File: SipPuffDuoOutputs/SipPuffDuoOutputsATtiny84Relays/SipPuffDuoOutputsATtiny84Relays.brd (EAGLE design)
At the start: 48 x 70 mm, 19 parts, among them U1 ATTINY84-20PU, U2 AQY212EH, U3 AQY212EH

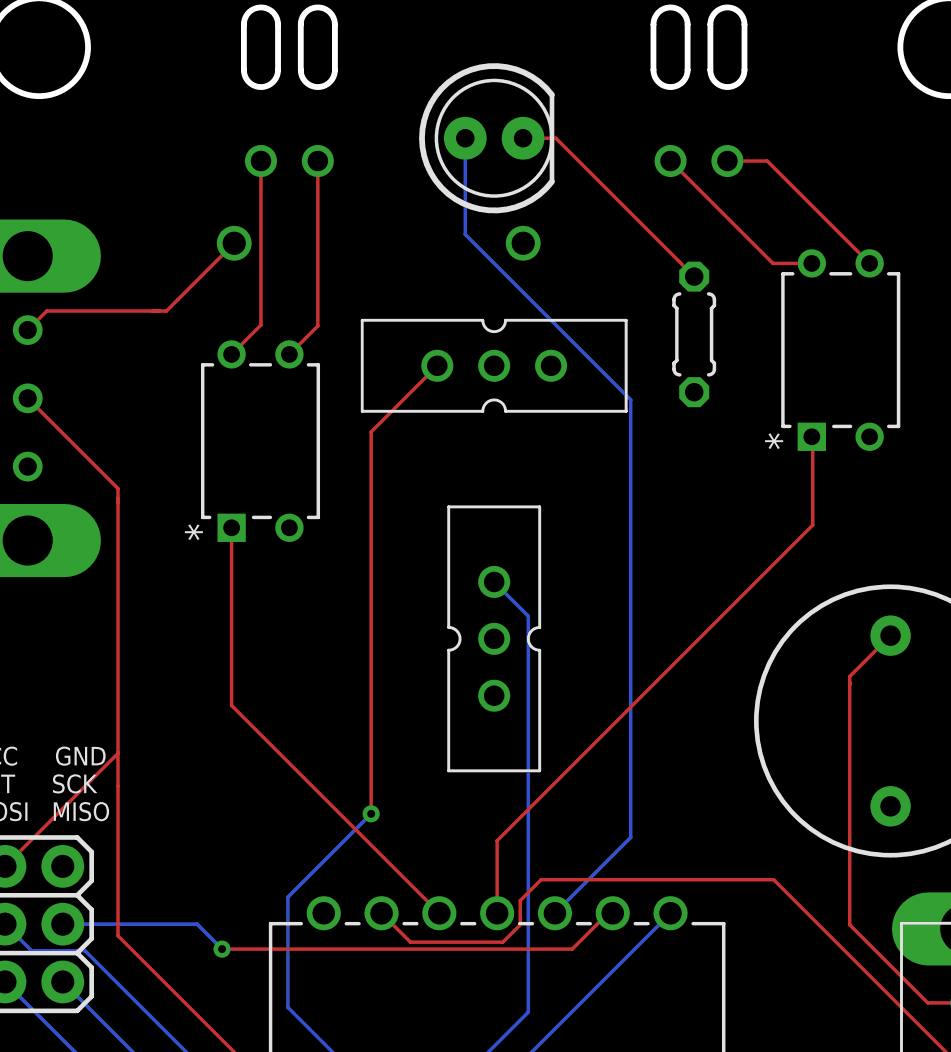
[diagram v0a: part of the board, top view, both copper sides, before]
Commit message: Changed resistors size
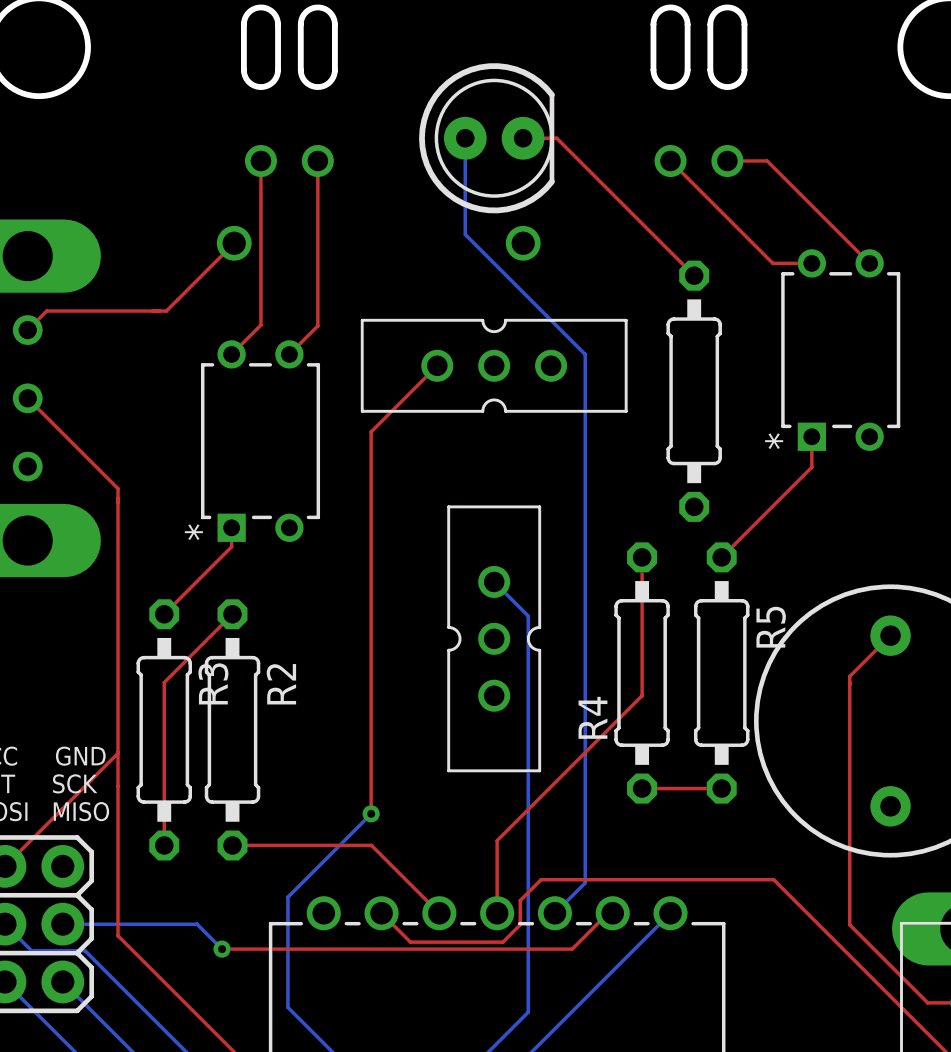
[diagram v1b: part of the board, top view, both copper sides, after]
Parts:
- added R2, R3, R4, R5: 1k, MMC Eagle:RESISTOR_0207/10
- R1: device MMC Eagle:RESISTOR_0204/5 -> MMC Eagle:RESISTOR_0207/10
- moved R1 2.50 mm to (32.8, 50.9)
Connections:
- new net N$19: R2.1, R3.2
- new net N$20: R3.1, U2.1
- new net N$21: R4.1, R5.2
- new net N$22: R5.1, U3.1
- net N$2: now also R2.2; no longer U2.1
- net N$4: now also R4.2; no longer U3.1
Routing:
- net N$19: track 0.00 -> 11.4 mm
- net N$2: track 20.7 -> 10.3 mm
- net N$4: track 26.7 -> 18.3 mm
- net N$22: track 0.00 -> 6.94 mm
- net N$20: track 0.00 -> 5.03 mm
- net N$21: track 0.00 -> 3.50 mm
- net N$1: track 38.5 -> 36.8 mm
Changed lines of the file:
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@@
 <attribute name="VALUE" x="20.444" y="14.89" size="1.27" layer="27"/>
 </element>
-<element name="R1" library="MMC Eagle" library_urn="urn:adsk.eagle:library:3491419" package="RESISTOR_0204/5" package3d_urn="urn:adsk.eagle:package:3491543/2" value="1k" x="32.79" y="53.38" smashed="yes" rot="R90">
-<attribute name="VALUE" x="34.6014" y="52.7464" size="0.9906" layer="27" ratio="10" rot="R90"/>
+<element name="R1" library="MMC Eagle" library_urn="urn:adsk.eagle:library:3491419" package="RESISTOR_0207/10" package3d_urn="urn:adsk.eagle:package:5426338/2" value="1k" x="32.79" y="50.88" smashed="yes" rot="R90">
+<attribute name="VALUE" x="34.6014" y="50.2464" size="0.9906" layer="27" ratio="10" rot="R90"/>
 </element>
 <element name="U$1" library="MMC Eagle" library_urn="urn:adsk.eagle:library:3491419" package="2X3" package3d_urn="urn:adsk.eagle:package:4704386/2" value="HEADER_2X03" x="2.5" y="30" smashed="yes" rot="R270"/>
@@
 </element>
 <element name="U$5" library="MMC Eagle" library_urn="urn:adsk.eagle:library:3491419" package="1X02" package3d_urn="urn:adsk.eagle:package:4737896/2" value="HEADER_1X02" x="26.67" y="15.26" smashed="yes"/>
+<element name="R2" library="MMC Eagle" library_urn="urn:adsk.eagle:library:3491419" package="RESISTOR_0207/10" package3d_urn="urn:adsk.eagle:package:5426338/2" value="1k" x="12.5" y="36" rot="R270"/>
+<element name="R3" library="MMC Eagle" library_urn="urn:adsk.eagle:library:3491419" package="RESISTOR_0207/10" package3d_urn="urn:adsk.eagle:package:5426338/2" value="1k" x="9.5" y="36" rot="R270"/>
+<element name="R4" library="MMC Eagle" library_urn="urn:adsk.eagle:library:3491419" package="RESISTOR_0207/10" package3d_urn="urn:adsk.eagle:package:5426338/2" value="1k" x="30.5" y="38.5" rot="R90"/>
+<element name="R5" library="MMC Eagle" library_urn="urn:adsk.eagle:library:3491419" package="RESISTOR_0207/10" package3d_urn="urn:adsk.eagle:package:5426338/2" value="1k" x="34" y="38.5" rot="R270"/>
 </elements>
 <signals>
@@
 <contactref element="D1" pad="K"/>
 <contactref element="R1" pad="2"/>
-<wire x1="32.79" y1="55.92" x2="26.71" y2="62" width="0.1524" layer="1"/>
-<wire x1="26.71" y1="62" x2="25.27" y2="62" width="0.1524" layer="1"/>
+<wire x1="25.27" y1="62" x2="26.75" y2="62" width="0.1524" layer="1"/>
+<wire x1="26.75" y1="62" x2="32.79" y2="55.96" width="0.1524" layer="1"/>
 </signal>
 <signal name="N$1">
@@
 <contactref element="D1" pad="A"/>
 <wire x1="22.73" y1="62" x2="22.73" y2="57.77" width="0.1524" layer="16"/>
-<wire x1="22.73" y1="57.77" x2="30" y2="50.5" width="0.1524" layer="16"/>
-<wire x1="30" y1="50.5" x2="30" y2="31.27" width="0.1524" layer="16"/>
-<wire x1="30" y1="31.27" x2="26.67" y2="27.94" width="0.1524" layer="16"/>
+<wire x1="22.73" y1="57.77" x2="28" y2="52.5" width="0.1524" layer="16"/>
+<wire x1="28" y1="52.5" x2="28" y2="29.27" width="0.1524" layer="16"/>
+<wire x1="28" y1="29.27" x2="26.67" y2="27.94" width="0.1524" layer="16"/>
 </signal>
 <signal name="N$3">
@@
 <signal name="N$2">
 <contactref element="U1" pad="12"/>
-<contactref element="U2" pad="1"/>
-<wire x1="21.59" y1="27.94" x2="12.46" y2="37.07" width="0.1524" layer="1"/>
-<wire x1="12.46" y1="37.07" x2="12.46" y2="44.88" width="0.1524" layer="1"/>
+<contactref element="R2" pad="2"/>
+<wire x1="12.5" y1="30.92" x2="18.61" y2="30.92" width="0.1524" layer="1"/>
+<wire x1="18.61" y1="30.92" x2="21.59" y2="27.94" width="0.1524" layer="1"/>
 </signal>
 <signal name="N$4">
 <contactref element="U1" pad="11"/>
-<contactref element="U3" pad="1"/>
 <wire x1="24.13" y1="27.94" x2="24.13" y2="31.13" width="0.1524" layer="1"/>
-<wire x1="24.13" y1="31.13" x2="38" y2="45" width="0.1524" layer="1"/>
-<wire x1="38" y1="45" x2="38" y2="48.84" width="0.1524" layer="1"/>
-<wire x1="38" y1="48.84" x2="37.96" y2="48.88" width="0.1524" layer="1"/>
+<wire x1="24.13" y1="31.13" x2="30.5" y2="37.5" width="0.1524" layer="1"/>
+<contactref element="R4" pad="2"/>
+<wire x1="30.5" y1="43.58" x2="30.5" y2="37.5" width="0.1524" layer="1"/>
 </signal>
 <signal name="N$14">
@@
 <wire x1="29.21" y1="17.8" x2="29.21" y2="19.685" width="0.1524" layer="1"/>
 </signal>
+<signal name="N$19">
+<contactref element="R3" pad="2"/>
+<contactref element="R2" pad="1"/>
+<wire x1="9.5" y1="30.92" x2="9.5" y2="38.08" width="0.1524" layer="1"/>
+<wire x1="9.5" y1="38.08" x2="12.5" y2="41.08" width="0.1524" layer="1"/>
+</signal>
+<signal name="N$20">
+<contactref element="U2" pad="1"/>
+<contactref element="R3" pad="1"/>
+<wire x1="9.5" y1="41.08" x2="12.46" y2="44.04" width="0.1524" layer="1"/>
+<wire x1="12.46" y1="44.04" x2="12.46" y2="44.88" width="0.1524" layer="1"/>
+</signal>
+<signal name="N$21">
+<contactref element="R4" pad="1"/>
+<contactref element="R5" pad="2"/>
+<wire x1="30.5" y1="33.42" x2="34" y2="33.42" width="0.1524" layer="1"/>
+</signal>
+<signal name="N$22">
+<contactref element="R5" pad="1"/>
+<contactref element="U3" pad="1"/>
+<wire x1="34" y1="43.58" x2="37.96" y2="47.54" width="0.1524" layer="1"/>
+<wire x1="37.96" y1="47.54" x2="37.96" y2="48.88" width="0.1524" layer="1"/>
+</signal>
 </signals>
